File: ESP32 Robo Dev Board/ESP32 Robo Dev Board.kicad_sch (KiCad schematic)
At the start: 16 parts, among them U1 ESP32-S3-WROOM-1, U102 AMS1117-3.3

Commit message: First Finished Version 0.1.
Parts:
- added J1: (no value), symbol Connector_Generic:Conn_02x05_Counter_Clockwise
- renumbered C101 to C1, C102 to C2, Cen101 to Cen1, Cs101 to Cs1, D101 to D1, D102 to D2, E101 to E1, E102 to E2, J_A101 to J_A1, J_B101 to J_B1, R101 to R1, R102 to R2, Ren101 to Ren1, Rs101 to Rs1, U102 to U2
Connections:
- net +3V3: now also J1.10 (Pin_10)
- net GND: now also J1.9 (Pin_9)
- net L_Signal_A: now also U1.31 (GPIO38/FSPIWP/SUBSPIWP)
- net L_Signal_B: now also U1.32 (MTCK/GPIO39/CLK_OUT3/SUBSPICS1)
- net R_Signal_A: now also U1.34 (MTDI/GPIO41/CLK_OUT1)
- net R_Signal_B: now also U1.33 (MTDO/GPIO40/CLK_OUT2)
- net Boot: now reaches U1.27 (GPIO0/BOOT)
- net Boot: now also J1.8 (Pin_8)
- net Enable: now reaches U1.3 (EN)
- net Enable: now also J1.1 (Pin_1)
- net Rx: now reaches U1.36 (U0RXD/GPIO44/CLK_OUT2)
- net Rx: now also J1.3 (Pin_3)
- net Tx: now reaches U1.37 (U0TXD/GPIO43/CLK_OUT1)
- net Tx: now also J1.2 (Pin_2)
- no-connect marks 2 -> 6

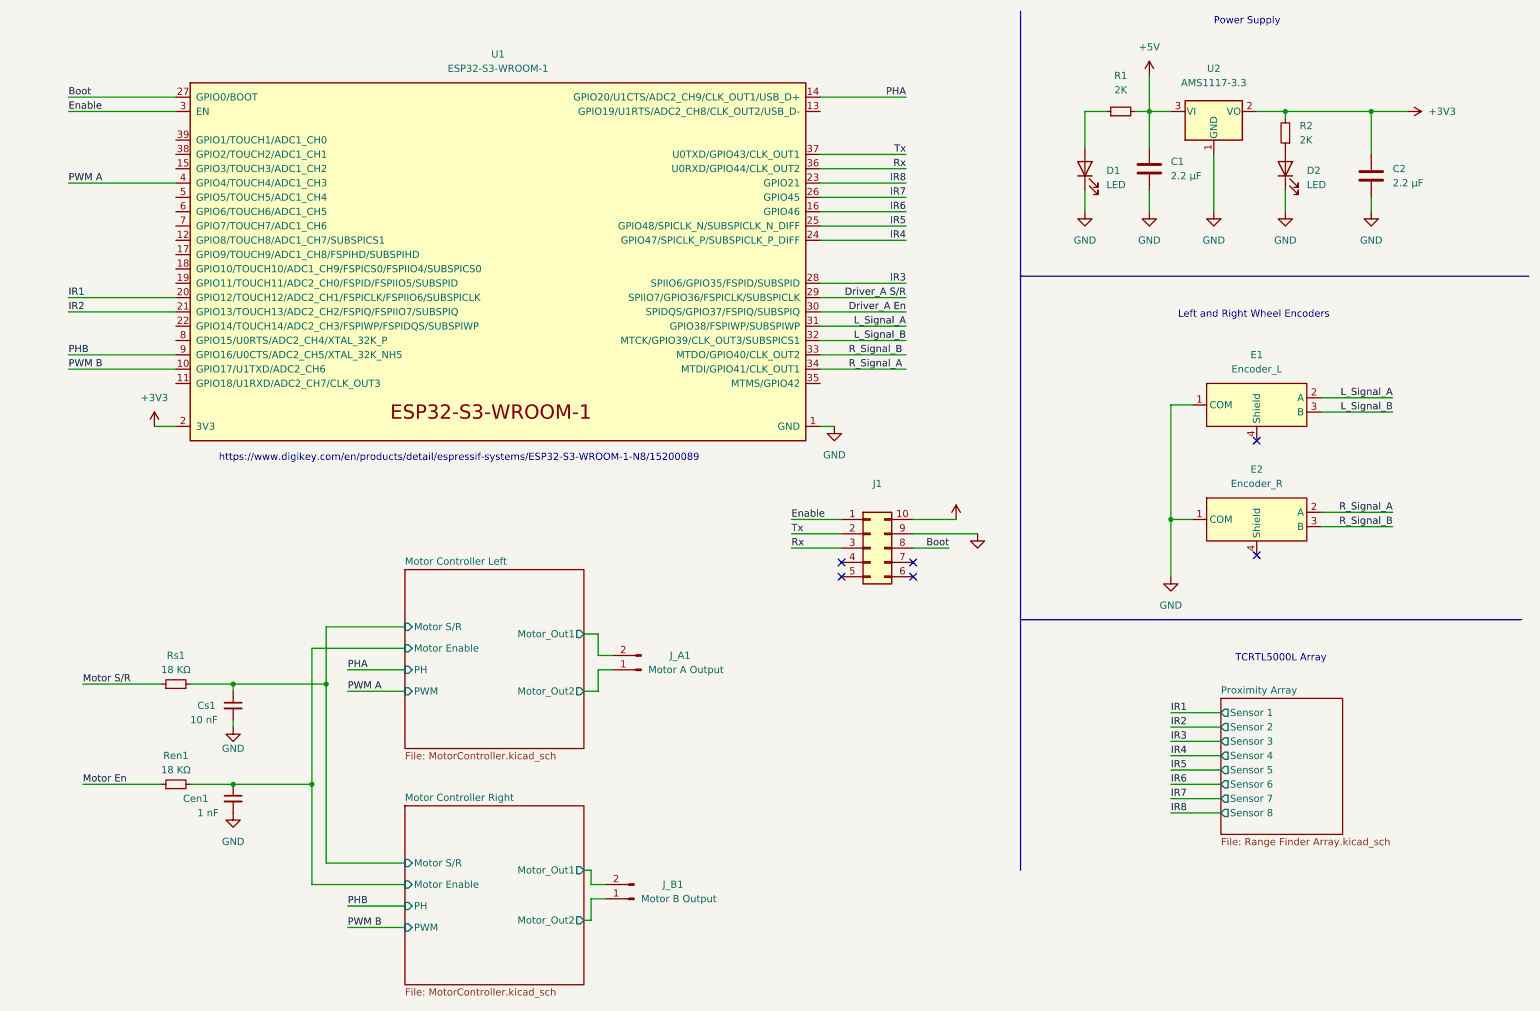
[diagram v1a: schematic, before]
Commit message: Add battery connector
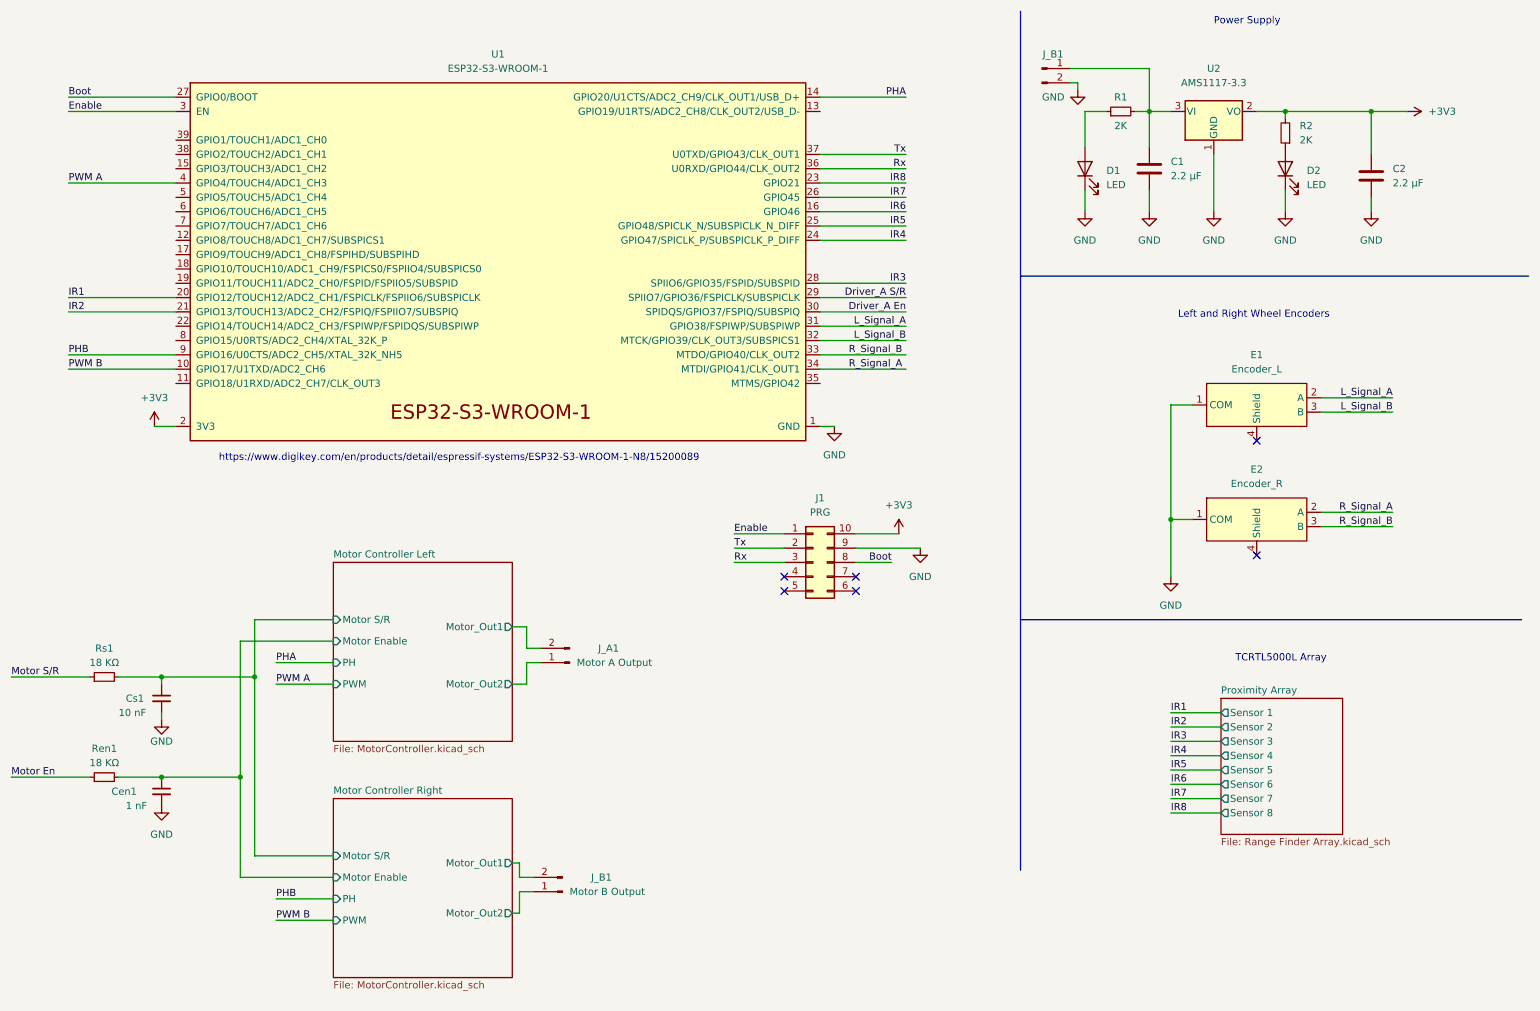
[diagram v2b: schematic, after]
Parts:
- added J_B1: (no value), symbol Connector:Conn_01x02_Male
- J1: value (none) -> PRG; footprint (none) -> Connector:Tag-Connect_TC2050-IDC-FP_2x05_P1.27mm_Vertical
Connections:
- net GND: now also J_B1.2 (Pin_2)
- net +5V: no longer names the net of C1.1, R1.2, U2.3 (VI)
- net +5V: now also J_B1.1 (Pin_1)
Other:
- moved on the sheet: Cen1, Cs1, J1, J_A1, J_B1, Ren1, Rs1

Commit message: update
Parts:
- renumbered J_B1 to J_B2
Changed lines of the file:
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@@
   (symbol (lib_id "power:GND") (at 207.01 48.26 0) (unit 1)
     (in_bom yes) (on_board yes) (fields_autoplaced)
-    (property "Reference" "#PWR07" (id 0) (at 207.01 54.61 0)
+    (property "Reference" "#PWR08" (id 0) (at 207.01 54.61 0)
       (effects (font (size 1.27 1.27)) hide)
     )
@@
   (symbol (lib_id "power:GND") (at 205.74 26.67 0) (unit 1)
     (in_bom yes) (on_board yes)
-    (property "Reference" "#PWR?" (id 0) (at 205.74 33.02 0)
+    (property "Reference" "#PWR07" (id 0) (at 205.74 33.02 0)
       (effects (font (size 1.27 1.27)) hide)
     )
@@
   (symbol (lib_id "Connector:Conn_01x02_Male") (at 199.39 22.86 0) (unit 1)
     (in_bom yes) (on_board yes)
-    (property "Reference" "J_B1" (id 0) (at 203.2 20.32 0)
+    (property "Reference" "J_B2" (id 0) (at 203.2 20.32 0)
       (effects (font (size 1.27 1.27)) (justify right))
     )
@@
       (reference "#PWR06") (unit 1) (value "GND") (footprint "")
     )
+    (path "/763b259e-f9f8-4217-9efd-65ca784f6851"
+      (reference "#PWR07") (unit 1) (value "GND") (footprint "")
+    )
     (path "/713083df-12bf-4081-9211-169792f90f86"
-      (reference "#PWR07") (unit 1) (value "GND") (footprint "")
+      (reference "#PWR08") (unit 1) (value "GND") (footprint "")
     )
     (path "/2a967591-2c10-4303-bb18-7a855e4ea57c"
@@
       (reference "#PWR044") (unit 1) (value "GND") (footprint "")
     )
-    (path "/763b259e-f9f8-4217-9efd-65ca784f6851"
-      (reference "#PWR?") (unit 1) (value "GND") (footprint "")
-    )
     (path "/8f68081f-33f7-4342-b1f0-d2938b6c2bf0"
       (reference "C1") (unit 1) (value "2.2 µF") (footprint "Capacitor_SMD:C_0805_2012Metric")
@@
     )
     (path "/a3149699-8a34-42d1-ac77-5fe843d39d26"
-      (reference "J_B1") (unit 1) (value "Batt In") (footprint "Connector_JST:JST_EH_B2B-EH-A_1x02_P2.50mm_Vertical")
+      (reference "J_B2") (unit 1) (value "Batt In") (footprint "Connector_JST:JST_EH_B2B-EH-A_1x02_P2.50mm_Vertical")
     )
     (path "/b9644345-2c8d-4f54-9d32-2353cd6b3881"
